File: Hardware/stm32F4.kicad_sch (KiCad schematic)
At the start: 30 parts, among them J1 USB_C_Receptacle_USB2.0_16P, J2 Conn_01x04, J5 Conn_01x20, J6 Conn_01x20, SW1 Push, SW3 Push, U1 STM32F411CCU6, U2 AMS1117-3.3, U4 2SC6, Y2 8MHz

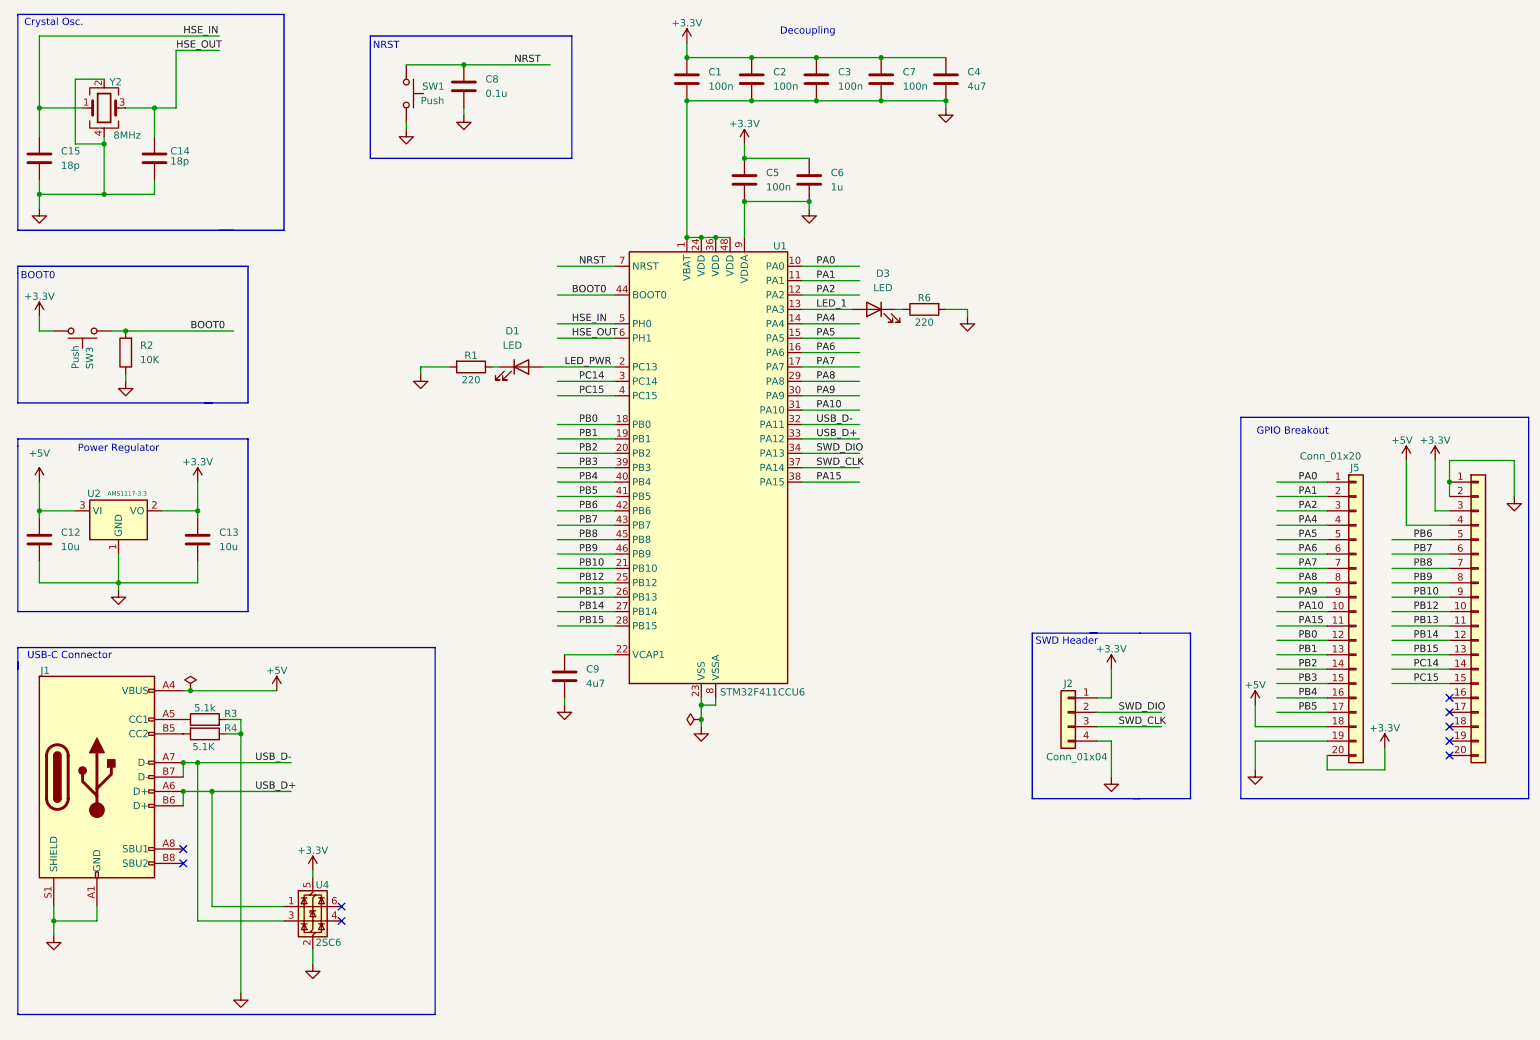
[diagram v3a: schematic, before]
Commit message: PCB Layout Rough Draft and Schematic Changes
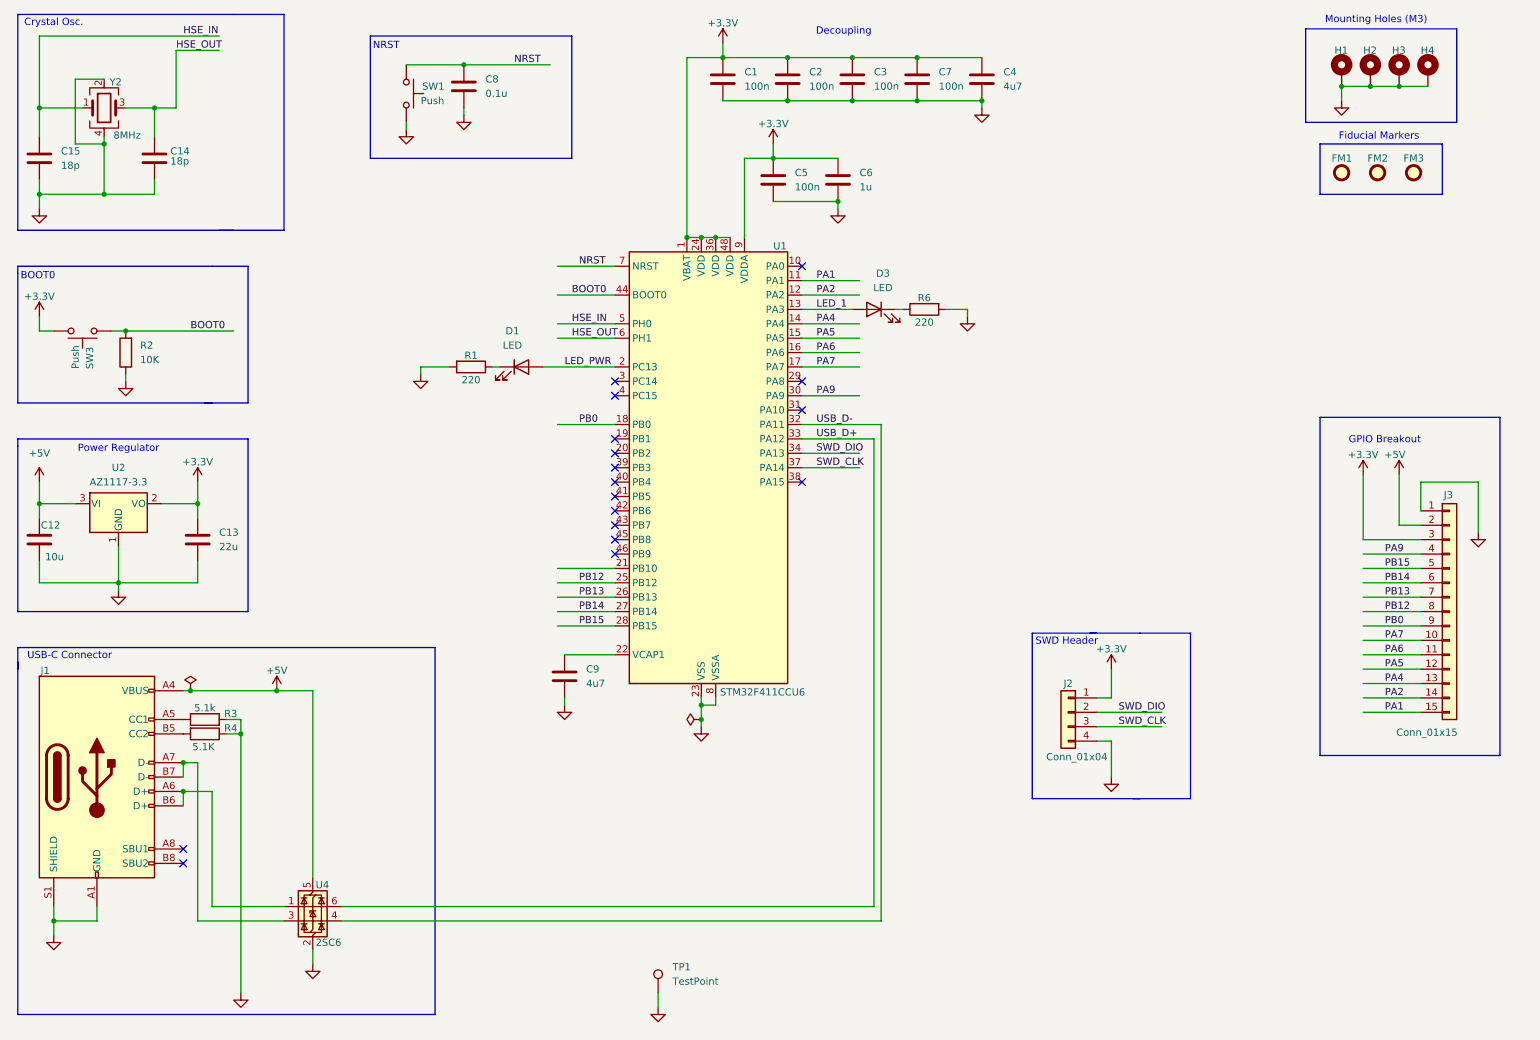
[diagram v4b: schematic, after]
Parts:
- removed J5, J6: Conn_01x20, Connector_PinHeader_2.54mm:PinHeader_1x20_P2.54mm_Vertical, symbol Connector_Generic:Conn_01x20
- removed U2: AMS1117-3.3, Package_TO_SOT_SMD:SOT-223-3_TabPin2, symbol Regulator_Linear:AMS1117-3.3
- added FM1, FM2, FM3: Fiducial, Fiducial:Fiducial_1mm_Mask2mm, symbol Mechanical:Fiducial
- added H1, H2, H3, H4: MountingHole_Pad, MountingHole:MountingHole_2.2mm_M2_Pad_Via, symbol Mechanical:MountingHole_Pad
- added J3: Conn_01x15, Connector_PinHeader_2.54mm:PinHeader_1x15_P2.54mm_Vertical, symbol Connector_Generic:Conn_01x15
- added TP1: TestPoint, TestPoint:TestPoint_Bridge_Pitch2.54mm_Drill0.7mm, symbol Connector:TestPoint
- added U2: AZ1117-3.3, Package_TO_SOT_SMD:SOT-223-3_TabPin2, symbol Regulator_Linear:AZ1117-3.3
- C13: value 10u -> 22u; footprint Capacitor_SMD:C_0402_1005Metric -> Capacitor_SMD:C_0603_1608Metric; Distributor Link https://www.digikey.com/en/products/detail/nextgen-componen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 -> https://www.digikey.com/en/products/detail/murata-electroni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; Manufacturer Aillen -> Murata Electronics; Manufacturer Part Number 0402W106M6R3HI -> GRM188R60J226MEA0D
- C15: footprint Capacitor_SMD:C_0402_1005Metric -> Capacitor_SMD:C_0603_1608Metric
- J2: footprint Connector_PinHeader_1.27mm:PinHeader_1x04_P1.27mm_Horizontal -> Connector_PinHeader_1.27mm:PinHeader_1x04_P1.27mm_Vertical; Distributor Link https://www.digikey.com/en/products/detail/sullins-connector-solutions/GRPB041VWCN-RC/1786467 -> https://www.digikey.com/en/products/detail/sullins-connector-solutions/GRPB041VWVN-RC/1786440; Manufacturer Part Number GRPB041VWCN-RC -> GRPB041VWVN-RC
- SW1, SW3: footprint Button_Switch_SMD:SW_SPST_CK_RS282G05A3 -> Button_Switch_SMD:SW_SPST_B3U-1000P; Distributor Link https://www.digikey.com/en/products/detail/c-k/RS-282G05A3-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 -> https://www.digikey.com/en/products/detail/omron-electronic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; Manufacturer C&K -> Omron Electronics Inc-EMC Div; Manufacturer Part Number RS-282G05A3-SM RT -> B3U-1000P-B
- Y2: footprint Crystal:Crystal_HC49-4H_Vertical -> Crystal:Crystal_SMD_Abracon_ABM3B-4Pin_5.0x3.2mm; Distributor Link https://www.digikey.com/en/products/detail/ecs-inc/ECS-080-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 -> https://www.digikey.com/en/products/detail/abracon-llc/ABM3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; Manufacturer ECS Inc. -> Abracon LLC; Manufacturer Part Number ECS-080-18-5PX-JES-TR -> ABM3B-8.000MHZ-B2-T
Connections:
- net +3.3V: now also U1.1 (VBAT), U1.24 (VDD), U1.36 (VDD), U1.48 (VDD), U1.9 (VDDA), J3.3 (Pin_3), U2.2 (VO); no longer U4.5 (VBUS)
- net +5V: now also U4.5 (VBUS), J3.2 (Pin_2), U2.3 (VI)
- net GND: now also H1.1, H2.1, H3.1, H4.1, J3.1 (Pin_1), TP1.1, U2.1 (GND); no longer U1.1 (VBAT), U1.24 (VDD), U1.36 (VDD), U1.48 (VDD), U1.9 (VDDA)
- net PA1: now also J3.15 (Pin_15)
- net PA2: now also J3.14 (Pin_14)
- net PA4: now also J3.13 (Pin_13)
- net PA5: now also J3.12 (Pin_12)
- net PA6: now also J3.11 (Pin_11)
- net PA7: now also J3.10 (Pin_10)
- net PA9: now also J3.4 (Pin_4)
- net PB0: now also J3.9 (Pin_9)
- net PB12: now also J3.8 (Pin_8)
- net PB13: now also J3.7 (Pin_7)
- net PB14: now also J3.6 (Pin_6)
- net PB15: now also J3.5 (Pin_5)
- net USB_D+: now also U4.6 (I/O1); no longer J1.A6 (D+), J1.B6 (D+), U4.1 (I/O1)
- net USB_D-: now also U4.4 (I/O2); no longer J1.A7 (D-), J1.B7 (D-), U4.3 (I/O2)
- net PA0: no longer names the net of U1.10 (PA0)
- net PA10: no longer names the net of U1.31 (PA10)
- net PA15: no longer names the net of U1.38 (PA15)
- net PA8: no longer names the net of U1.29 (PA8)
- net PB1: no longer names the net of U1.19 (PB1)
- net PB10: no longer names the net of U1.21 (PB10)
- net PB2: no longer names the net of U1.20 (PB2)
- net PB3: no longer names the net of U1.39 (PB3)
- net PB4: no longer names the net of U1.40 (PB4)
- net PB5: no longer names the net of U1.41 (PB5)
- net PB6: no longer names the net of U1.42 (PB6)
- net PB7: no longer names the net of U1.43 (PB7)
- net PB8: no longer names the net of U1.45 (PB8)
- net PB9: no longer names the net of U1.46 (PB9)
- net PC14: no longer names the net of U1.3 (PC14)
- net PC15: no longer names the net of U1.4 (PC15)
- new net: J1.A6 (D+), J1.B6 (D+), U4.1 (I/O1)
- new net: J1.A7 (D-), J1.B7 (D-), U4.3 (I/O2)
- no-connect marks 9 -> 17
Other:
- note added: "Fiducial Markers"
- note added: "Mounting Holes (M3)"
- moved on the sheet: C1, C2, C3, C4, C5, C6, C7
